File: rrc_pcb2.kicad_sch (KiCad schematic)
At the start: 18 parts, among them J1 battery_header, J2 buzzer_toggle_pin, U2 Teensy4.1, U3 BN220-GPS, U5 MS5611, U6 logo, U7 voltReg

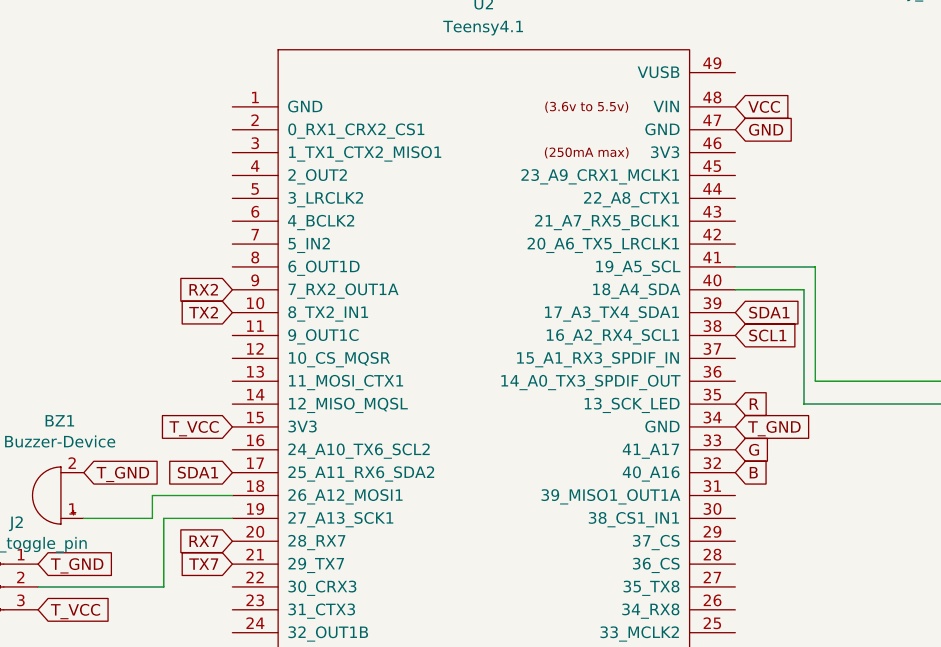
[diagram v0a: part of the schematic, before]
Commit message: edited led
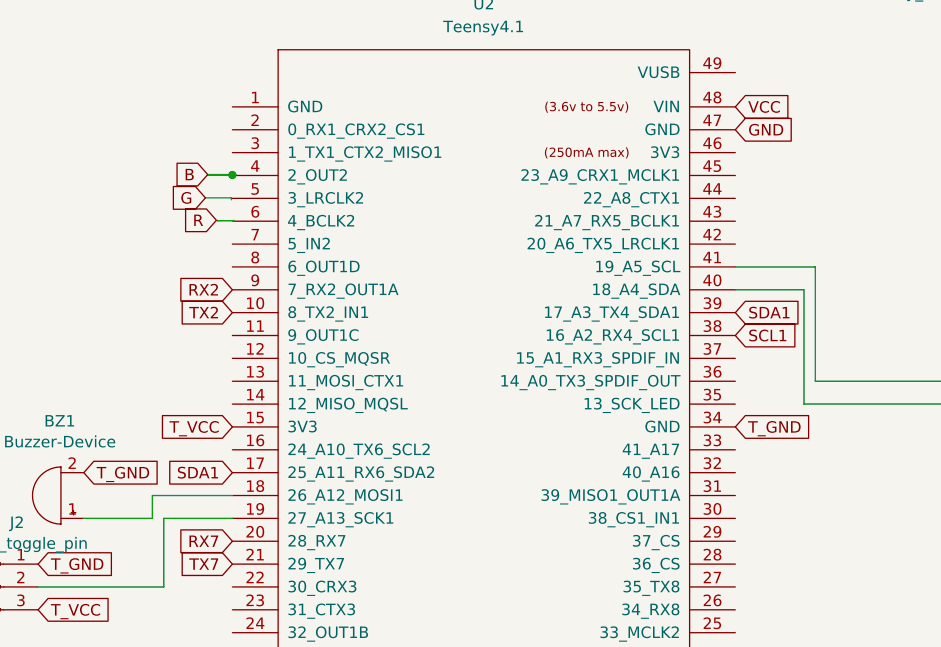
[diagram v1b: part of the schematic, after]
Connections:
- net B: no longer U2.32 (40_A16)
- net G: no longer U2.33 (41_A17)
- net R: no longer U2.35 (13_SCK_LED)
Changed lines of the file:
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@@
 (kicad_sch (version 20230121) (generator eeschema)
   (paper "A4")
+  (junction (at 99.06 29.1592) (diameter 0) (color 0 0 0 0)
+  )
+  (wire (pts (xy 99.1616 34.2392) (xy 97.3836 34.2392))
+    (stroke (width 0) (type default))
+  )
+  (wire (pts (xy 99.2124 34.1884) (xy 99.2124 34.29))
+    (stroke (width 0) (type default))
+  )
   (wire (pts (xy 241.3 105.41) (xy 229.87 105.41))
     (stroke (width 0) (type default))
@@
     (stroke (width 0) (type default))
   )
+  (wire (pts (xy 99.06 29.1592) (xy 99.1108 29.3116))
+    (stroke (width 0) (type default))
+  )
   (wire (pts (xy 200.66 16.51) (xy 234.95 16.51))
     (stroke (width 0) (type default))
@@
     (stroke (width 0) (type default))
   )
+  (wire (pts (xy 99.1108 29.1084) (xy 99.1108 29.1592))
+    (stroke (width 0) (type default))
+  )
   (wire (pts (xy 200.66 20.32) (xy 200.66 19.05))
     (stroke (width 0) (type default))
   )
+  (wire (pts (xy 96.0628 31.6992) (xy 98.9584 31.6992))
+    (stroke (width 0) (type default))
+  )
+  (wire (pts (xy 99.1108 29.1592) (xy 99.06 29.1592))
+    (stroke (width 0) (type default))
+  )
+  (wire (pts (xy 97.3836 34.1884) (xy 97.3836 34.2392))
+    (stroke (width 0) (type default))
+  )
   (wire (pts (xy 90.17 67.31) (xy 90.17 64.77))
     (stroke (width 0) (type default))
@@
     (stroke (width 0) (type default))
   )
+  (wire (pts (xy 99.06 34.29) (xy 99.2124 34.29))
+    (stroke (width 0) (type default))
+  )
   (wire (pts (xy 91.44 67.31) (xy 99.06 67.31))
     (stroke (width 0) (type default))
@@
     (stroke (width 0) (type default))
   )
+  (wire (pts (xy 96.3168 29.1084) (xy 99.1108 29.1084))
+    (stroke (width 0) (type default))
+  )
+  (wire (pts (xy 96.3168 29.1084) (xy 96.3168 29.1592))
+    (stroke (width 0) (type default))
+  )
   (wire (pts (xy 234.95 20.32) (xy 200.66 20.32))
     (stroke (width 0) (type default))
   )
+  (wire (pts (xy 98.9584 31.6992) (xy 98.9584 31.9024))
+    (stroke (width 0) (type default))
+  )
   (wire (pts (xy 163.83 52.07) (xy 180.34 52.07))
     (stroke (width 0) (type default))
@@
   )
   (wire (pts (xy 90.17 64.77) (xy 99.06 64.77))
+    (stroke (width 0) (type default))
+  )
+  (wire (pts (xy 96.3168 29.1592) (xy 99.06 29.1592))
     (stroke (width 0) (type default))
   )
@@
     )
   )
-  (global_label "G" (shape input) (at 154.94 59.69 0) (fields_autoplaced)
-    (effects (font (size 1.27 1.27)) (justify left))
-    (property "Intersheetrefs" "${INTERSHEET_REFS}" (at 158.541 59.69 0)
-      (effects (font (size 1.27 1.27)) (justify left) hide)
-    )
-  )
   (global_label "T_GND" (shape input) (at 241.3 100.33 180) (fields_autoplaced)
     (effects (font (size 1.27 1.27)) (justify right))
@@
     )
   )
+  (global_label "R" (shape input) (at 97.282 34.1884 180) (fields_autoplaced)
+    (effects (font (size 1.27 1.27)) (justify right))
+    (property "Intersheetrefs" "${INTERSHEET_REFS}" (at 93.681 34.1884 0)
+      (effects (font (size 1.27 1.27)) (justify right) hide)
+    )
+  )
   (global_label "RX7" (shape input) (at 99.06 69.85 180) (fields_autoplaced)
     (effects (font (size 1.27 1.27)) (justify right))
@@
     )
   )
-  (global_label "B" (shape input) (at 154.94 62.23 0) (fields_autoplaced)
-    (effects (font (size 1.27 1.27)) (justify left))
-    (property "Intersheetrefs" "${INTERSHEET_REFS}" (at 158.541 62.23 0)
-      (effects (font (size 1.27 1.27)) (justify left) hide)
+  (global_label "B" (shape input) (at 96.3168 29.1084 180) (fields_autoplaced)
+    (effects (font (size 1.27 1.27)) (justify right))
+    (property "Intersheetrefs" "${INTERSHEET_REFS}" (at 92.7158 29.1084 0)
+      (effects (font (size 1.27 1.27)) (justify right) hide)
     )
   )
@@
     )
   )
-  (global_label "R" (shape input) (at 154.94 54.61 0) (fields_autoplaced)
-    (effects (font (size 1.27 1.27)) (justify left))
-    (property "Intersheetrefs" "${INTERSHEET_REFS}" (at 158.541 54.61 0)
-      (effects (font (size 1.27 1.27)) (justify left) hide)
-    )
-  )
   (global_label "T_VCC" (shape input) (at 222.25 105.41 180) (fields_autoplaced)
     (effects (font (size 1.27 1.27)) (justify right))
     (property "Intersheetrefs" "${INTERSHEET_REFS}" (at 307.34 171.45 0)
       (effects (font (size 1.27 1.27)) hide)
+    )
+  )
+  (global_label "G" (shape input) (at 96.0628 31.6992 180) (fields_autoplaced)
+    (effects (font (size 1.27 1.27)) (justify right))
+    (property "Intersheetrefs" "${INTERSHEET_REFS}" (at 92.4618 31.6992 0)
+      (effects (font (size 1.27 1.27)) (justify right) hide)
     )
   )
@@
     )
     (pin "1")
+    (pin "2")
+    (pin "3")
     (pin "4")
-    (pin "2")
-    (pin "3")
     (instances
       (project "rrc_pcb2"
@@
       (effects (font (size 1.27 1.27)) hide)
     )
+    (pin "1")
+    (pin "2")
+    (pin "3")
     (pin "4")
-    (pin "1")
     (pin "5")
+    (pin "6")
     (pin "7")
-    (pin "2")
-    (pin "3")
-    (pin "6")
     (pin "8")
     (instances

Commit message: INA260
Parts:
- added U1: INA260, INA260:INA260, symbol parts:INA260
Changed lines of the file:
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@@
+    )
+  )
+  (symbol (lib_id "parts:INA260") (at 71.12 132.08 0) (unit 1)
+    (in_bom yes) (on_board yes) (dnp no) (fields_autoplaced)
+    (property "Reference" "U1" (at 73.4712 134.62 0)
+      (effects (font (size 1.524 1.524)) (justify left))
+    )
+    (property "Value" "INA260" (at 73.4712 137.16 0)
+      (effects (font (size 1.524 1.524)) (justify left))
+    )
+    (property "Footprint" "INA260:INA260" (at 69.85 128.27 0)
+      (effects (font (size 1.524 1.524)) hide)
+    )
+    (property "Datasheet" "" (at 71.12 132.08 0)
+      (effects (font (size 1.524 1.524)))
+    )
+    (pin "1")
+    (pin "10")
+    (pin "2")
+    (pin "3")
+    (pin "4")
+    (pin "5")
+    (pin "6")
+    (pin "7")
+    (pin "8")
+    (pin "9")
+    (instances
+      (project "rrc_pcb2"
+        (path "/03c52831-5dc5-43c5-a442-8d23643b46fb"
+          (reference "U1") (unit 1)
+        )
+      )
     )
   )
